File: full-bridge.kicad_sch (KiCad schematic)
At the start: 14 parts, among them U801 VNH7070ASTR

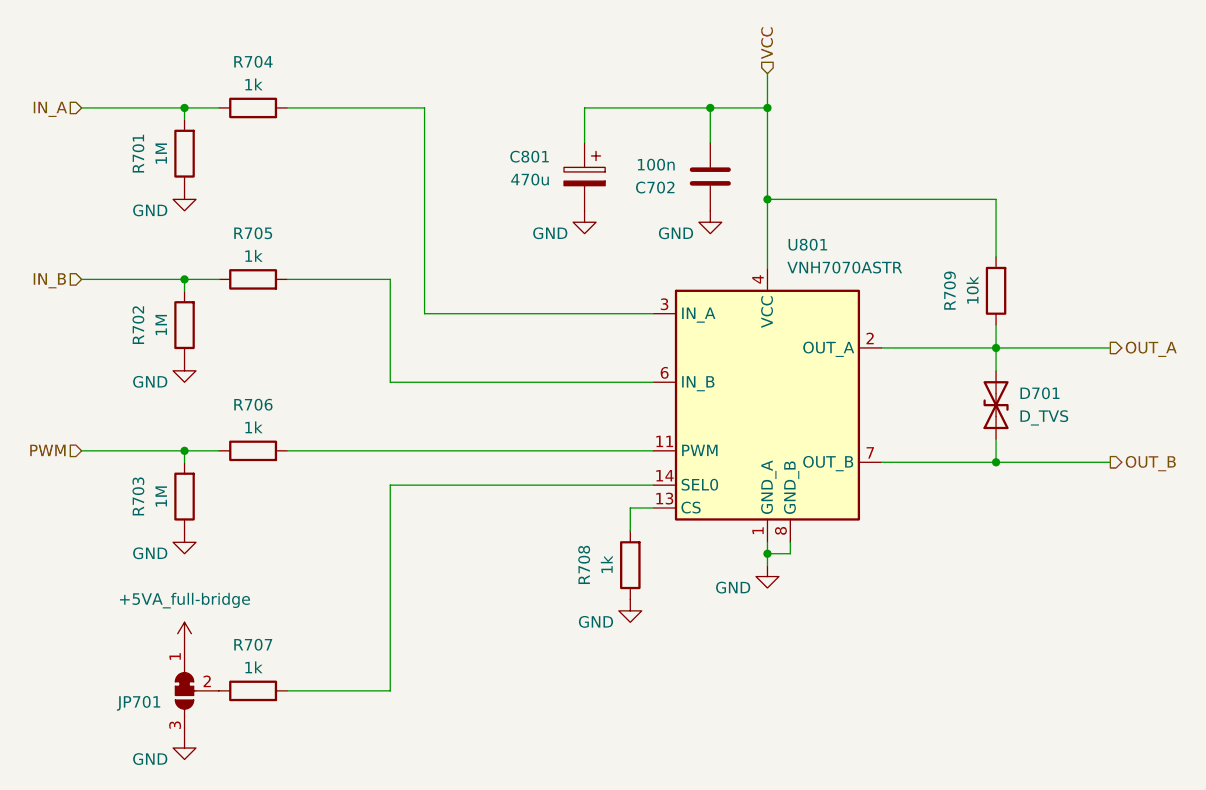
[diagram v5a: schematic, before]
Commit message: add full-bridge sub layout
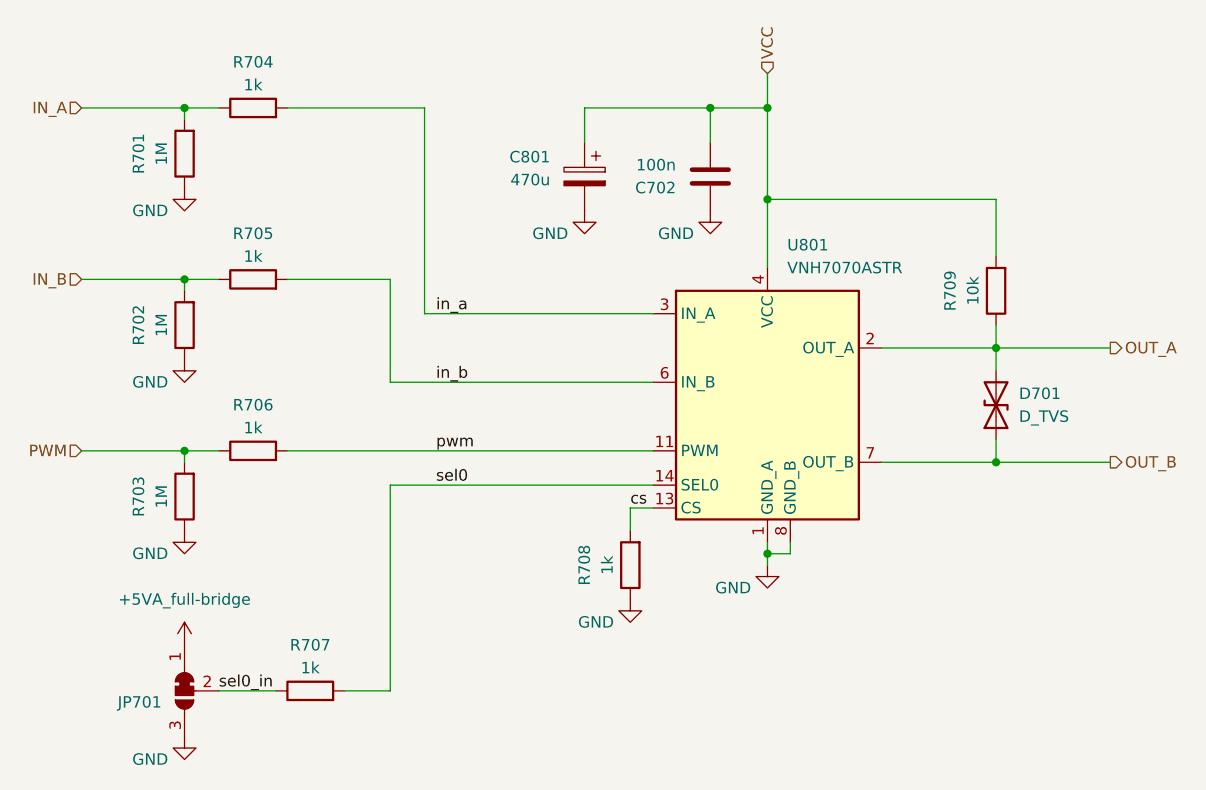
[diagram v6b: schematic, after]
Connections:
- net pwm: now reaches R706.2, U801.11 (PWM)
- net sel0_in: now reaches JP701.2 (C), R707.1
- net cs: now reaches R708.2, U801.13 (CS)
- net sel0: now reaches R707.2, U801.14 (SEL0)
- net in_a: now reaches R704.2, U801.3 (IN_A)
- net in_b: now reaches R705.2, U801.6 (IN_B)
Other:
- moved on the sheet: R707
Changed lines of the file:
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@@
+	(wire
+		(pts
+			(xy 97.79 139.7) (xy 91.44 139.7)
+		)
+		(stroke
+			(width 0)
+			(type default)
+		)
+	)
 	(wire
 		(pts
@@
 	(wire
 		(pts
-			(xy 99.06 139.7) (xy 110.49 139.7)
+			(xy 105.41 139.7) (xy 110.49 139.7)
 		)
 		(stroke
@@
 			(width 0)
 			(type default)
+		)
+	)
+	(label "sel0"
+		(at 115.57 116.84 0)
+		(fields_autoplaced yes)
+		(effects
+			(font
+				(size 1.27 1.27)
+			)
+			(justify left bottom)
+		)
+	)
+	(label "sel0_in"
+		(at 91.44 139.7 0)
+		(fields_autoplaced yes)
+		(effects
+			(font
+				(size 1.27 1.27)
+			)
+			(justify left bottom)
+		)
+	)
+	(label "in_b"
+		(at 115.57 105.41 0)
+		(fields_autoplaced yes)
+		(effects
+			(font
+				(size 1.27 1.27)
+			)
+			(justify left bottom)
+		)
+	)
+	(label "in_a"
+		(at 115.57 97.79 0)
+		(fields_autoplaced yes)
+		(effects
+			(font
+				(size 1.27 1.27)
+			)
+			(justify left bottom)
+		)
+	)
+	(label "pwm"
+		(at 115.57 113.03 0)
+		(fields_autoplaced yes)
+		(effects
+			(font
+				(size 1.27 1.27)
+			)
+			(justify left bottom)
+		)
+	)
+	(label "cs"
+		(at 137.16 119.38 0)
+		(fields_autoplaced yes)
+		(effects
+			(font
+				(size 1.27 1.27)
+			)
+			(justify left bottom)
 		)
 	)
@@
 	(symbol
 		(lib_id "enclosure:R")
-		(at 95.25 139.7 90)
+		(at 101.6 139.7 90)
 		(unit 1)
 		(exclude_from_sim no)
@@
 		(dnp no)
 		(property "Reference" "R707"
-			(at 95.25 134.62 90)
+			(at 101.6 134.62 90)
 			(effects
 				(font
@@
 		)
 		(property "Value" "1k"
-			(at 95.25 137.16 90)
+			(at 101.6 137.16 90)
 			(effects
 				(font
@@
 		)
 		(property "Footprint" "enclosure:R_1210_3225Metric_Pad1.30x2.65mm_HandSolder"
-			(at 95.25 141.478 90)
+			(at 101.6 141.478 90)
 			(effects
 				(font
@@
 		)
 		(property "Datasheet" "./datasheet/R_SMD_Yageo.pdf"
-			(at 95.25 139.7 0)
+			(at 101.6 139.7 0)
 			(effects
 				(font
@@
 		)
 		(property "Description" "Resistor"
-			(at 95.25 139.7 0)
+			(at 101.6 139.7 0)
 			(effects
 				(font
@@
 		)
 		(property "MPN" "RC1210FR-071KL"
-			(at 95.25 139.7 0)
+			(at 101.6 139.7 0)
 			(effects
 				(font
@@
 		)
 		(property "VPN" "603-RC1210FR-071KL"
-			(at 95.25 139.7 0)
-			(effects
-				(font
+			(at 101.6 139.7 0)
+			(effects
+				(font
